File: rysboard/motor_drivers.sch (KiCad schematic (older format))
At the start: 26 parts, among them J15 Microfit_1x4, J16 Microfit_1x4, U2 ST L6470 28Pin, U3 ST L6470 28Pin

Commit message: rysboard: schematic cleanup done after kicad import
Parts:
- removed C10, C11: 47u, Capacitor_Tantalum_SMD:CP_EIA-7343-31_Kemet-D, symbol Device:CP
- removed C12, C2, C5, C6: 100n, Capacitor_SMD:C_0603_1608Metric, symbol Device:C
- removed C16: 220n, Capacitor_SMD:C_0805_2012Metric, symbol Device:C
- removed C3: 10u, Capacitor_SMD:C_1206_3216Metric, symbol Device:C
- removed J16: Microfit_1x4, Connector_Molex:Molex_Micro-Fit_3.0_43650-0415_1x04_P3.00mm_Vertical, symbol rysboard:Microfit_1x4
- removed R4: 27k1%, Resistor_SMD:R_0603_1608Metric, symbol Device:R
- removed U3: ST L6470 28Pin, symbol rysboard:ST_L6470_28Pin
- added C10: 10n, Capacitor_SMD:C_0603_1608Metric, symbol Device:C
- added C11: 100n, Capacitor_SMD:C_0603_1608Metric, symbol Device:C
- added C12, C13: 47u, Capacitor_Tantalum_SMD:CP_EIA-7343-31_Kemet-D, symbol Device:CP
- added C8: 10u, Capacitor_SMD:C_1206_3216Metric, symbol Device:C
- added C9: 220n, Capacitor_SMD:C_0805_2012Metric, symbol Device:C
- added J3: Motor R, Connector_Molex:Molex_Micro-Fit_3.0_43650-0415_1x04_P3.00mm_Vertical, symbol rysboard:Microfit_1x4
- added R1, R2: 10k, Resistor_SMD:R_0603_1608Metric, symbol Device:R
- added R5: 27k1%, Resistor_SMD:R_0603_1608Metric, symbol Device:R
- added U2: L6470, Package_SO:HTSSOP-28-1EP_4.4x9.7mm_P0.65mm_EP3.4x9.5mm_ThermalVias, symbol rysboard:ST_L6470_HTSSOP28
- C14: value 10u -> 100n; footprint Capacitor_SMD:C_1206_3216Metric -> Capacitor_SMD:C_0603_1608Metric
- C3: renamed from C13; value 10u -> 10n; footprint Capacitor_SMD:C_1206_3216Metric -> Capacitor_SMD:C_0603_1608Metric
- J2: renamed from J15; value Microfit_1x4 -> Motor L
- U1: renamed from U2; value ST L6470 28Pin -> L6470; footprint (none) -> Package_SO:HTSSOP-28-1EP_4.4x9.7mm_P0.65mm_EP3.4x9.5mm_ThermalVias; symbol rysboard:ST_L6470_28Pin -> rysboard:ST_L6470_HTSSOP28
- renumbered C15 to C2, C7 to C5, C8 to C6, C9 to C7, R5 to R4
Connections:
- net labels removed: VBOOT0, VBOOT1
- wire segments 124 -> 119
- no-connect marks 8 -> 6
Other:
- note added: "Pull-ups for STANDBY and BUSY flags (active low)"
- note removed: "Sterowniki silników krokowych"
- moved on the sheet: C2, C3, C5, C6, C7, D1, R3, R4

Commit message: rysboard: library cleanup, fix bad connector references
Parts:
- J2, J3: symbol rysboard:Microfit_1x4 -> Connector_Generic:Conn_01x04
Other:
- moved on the sheet: C13, C14, C6, C7
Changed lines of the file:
@@
 L Device:CP C6
 U 1 1 5EB9B840
-P 5175 3900
-F 0 "C6" H 5275 3910 60  0000 L BNN
-F 1 "47u" H 5275 3810 60  0000 L BNN
-F 2 "Capacitor_Tantalum_SMD:CP_EIA-7343-31_Kemet-D" H 5275 3810 60  0001 C CNN
-F 3 "" H 5275 3810 60  0000 C CNN
-	1    5175 3900
+P 5225 3900
+F 0 "C6" H 5325 3910 60  0000 L BNN
+F 1 "47u" H 5325 3810 60  0000 L BNN
+F 2 "Capacitor_Tantalum_SMD:CP_EIA-7343-31_Kemet-D" H 5325 3810 60  0001 C CNN
+F 3 "" H 5325 3810 60  0000 C CNN
+	1    5225 3900
 	1    0    0    -1
 $EndComp
@@
 L power:Vdrive #PWR09
 U 1 1 5E96DF0C
-P 5000 3450
-F 0 "#PWR09" H 4800 3300 50  0001 C CNN
-F 1 "Vdrive" H 5017 3623 50  0000 C CNN
-F 2 "" H 5000 3450 50  0001 C CNN
-F 3 "" H 5000 3450 50  0001 C CNN
-	1    5000 3450
+P 5025 3450
+F 0 "#PWR09" H 4825 3300 50  0001 C CNN
+F 1 "Vdrive" H 5042 3623 50  0000 C CNN
+F 2 "" H 5025 3450 50  0001 C CNN
+F 3 "" H 5025 3450 50  0001 C CNN
+	1    5025 3450
 	1    0    0    -1
 $EndComp
@@
 L Device:C C7
 U 1 1 5E95E4E7
-P 5500 3900
-F 0 "C7" H 5600 3925 60  0000 L BNN
-F 1 "100n" H 5600 3825 60  0000 L BNN
-F 2 "Capacitor_SMD:C_0603_1608Metric" H 5400 3990 60  0001 C CNN
-F 3 "" H 5400 3990 60  0001 C CNN
-	1    5500 3900
-	1    0    0    -1
-$EndComp
-Wire Wire Line
-	5000 3550 5000 3450
+P 5600 3900
+F 0 "C7" H 5700 3925 60  0000 L BNN
+F 1 "100n" H 5700 3825 60  0000 L BNN
+F 2 "Capacitor_SMD:C_0603_1608Metric" H 5500 3990 60  0001 C CNN
+F 3 "" H 5500 3990 60  0001 C CNN
+	1    5600 3900
+	1    0    0    -1
+$EndComp
+Wire Wire Line
+	5025 3550 5025 3450
 $Comp
 L Device:R R4
@@
 L power:GND #PWR010
 U 1 1 5E9B3268
-P 5000 4250
-F 0 "#PWR010" H 5000 4000 50  0001 C CNN
-F 1 "GND" H 5005 4077 50  0000 C CNN
-F 2 "" H 5000 4250 50  0001 C CNN
-F 3 "" H 5000 4250 50  0001 C CNN
-	1    5000 4250
+P 5025 4250
+F 0 "#PWR010" H 5025 4000 50  0001 C CNN
+F 1 "GND" H 5030 4077 50  0000 C CNN
+F 2 "" H 5025 4250 50  0001 C CNN
+F 3 "" H 5025 4250 50  0001 C CNN
+	1    5025 4250
 	1    0    0    -1
 $EndComp
@@
 Connection ~ 4825 3550
 Wire Wire Line
-	4825 3550 5000 3550
-Wire Wire Line
-	5175 3750 5175 3550
-Wire Wire Line
-	5500 3750 5500 3550
-Wire Wire Line
-	5500 3550 5175 3550
-Connection ~ 5175 3550
-Connection ~ 5000 3550
-Wire Wire Line
-	5000 3550 5175 3550
+	4825 3550 5025 3550
+Wire Wire Line
+	5225 3750 5225 3550
+Wire Wire Line
+	5600 3750 5600 3550
+Wire Wire Line
+	5600 3550 5225 3550
+Connection ~ 5225 3550
+Connection ~ 5025 3550
+Wire Wire Line
+	5025 3550 5225 3550
 Wire Wire Line
 	4825 4050 4825 4250
 Connection ~ 4825 4250
 Wire Wire Line
-	4825 4250 5000 4250
-Wire Wire Line
-	5500 4050 5500 4250
-Wire Wire Line
-	5500 4250 5175 4250
-Connection ~ 5000 4250
-Wire Wire Line
-	5175 4050 5175 4250
-Connection ~ 5175 4250
-Wire Wire Line
-	5175 4250 5000 4250
+	4825 4250 5025 4250
+Wire Wire Line
+	5600 4050 5600 4250
+Wire Wire Line
+	5600 4250 5225 4250
+Connection ~ 5025 4250
+Wire Wire Line
+	5225 4050 5225 4250
+Connection ~ 5225 4250
+Wire Wire Line
+	5225 4250 5025 4250
 Wire Wire Line
 	4425 3850 4425 3900
@@
 	4425 3900 4425 3950
 $Comp
-L rysboard:Microfit_1x4 J2
+L Connector_Generic:Conn_01x04 J2
 U 1 1 5EB6E00E
-P 4575 2250
-F 0 "J2" H 4625 2000 60  0000 R TNN
-F 1 "Motor L" H 4625 2500 60  0000 R BNN
-F 2 "Connector_Molex:Molex_Micro-Fit_3.0_43650-0415_1x04_P3.00mm_Vertical" H 4825 2400 60  0001 C CNN
-F 3 "" H 4825 2400 60  0001 C CNN
-	1    4575 2250
-	-1   0    0    1
+P 4525 2200
+F 0 "J2" H 4525 2375 50  0000 C CNN
+F 1 "Motor L" H 4525 1900 50  0000 C CNN
+F 2 "Connector_Molex:Molex_Micro-Fit_3.0_43650-0415_1x04_P3.00mm_Vertical" H 4775 2350 50  0001 C CNN
+F 3 "" H 4775 2350 50  0001 C CNN
+	1    4525 2200
+	1    0    0    -1
 $EndComp
 Wire Wire Line
@@
 L Device:CP C13
 U 1 1 5EAE3CD8
-P 9675 3900
-F 0 "C13" H 9775 3910 60  0000 L BNN
-F 1 "47u" H 9775 3810 60  0000 L BNN
-F 2 "Capacitor_Tantalum_SMD:CP_EIA-7343-31_Kemet-D" H 9775 3810 60  0001 C CNN
-F 3 "" H 9775 3810 60  0000 C CNN
-	1    9675 3900
+P 9725 3900
+F 0 "C13" H 9825 3910 60  0000 L BNN
+F 1 "47u" H 9825 3810 60  0000 L BNN
+F 2 "Capacitor_Tantalum_SMD:CP_EIA-7343-31_Kemet-D" H 9825 3810 60  0001 C CNN
+F 3 "" H 9825 3810 60  0000 C CNN
+	1    9725 3900
 	1    0    0    -1
 $EndComp
@@
 L power:Vdrive #PWR015
 U 1 1 5EAE3CE4
-P 9500 3450
-F 0 "#PWR015" H 9300 3300 50  0001 C CNN
-F 1 "Vdrive" H 9517 3623 50  0000 C CNN
-F 2 "" H 9500 3450 50  0001 C CNN
-F 3 "" H 9500 3450 50  0001 C CNN
-	1    9500 3450
+P 9525 3450
+F 0 "#PWR015" H 9325 3300 50  0001 C CNN
+F 1 "Vdrive" H 9542 3623 50  0000 C CNN
+F 2 "" H 9525 3450 50  0001 C CNN
+F 3 "" H 9525 3450 50  0001 C CNN
+	1    9525 3450
 	1    0    0    -1
 $EndComp
@@
 L Device:C C14
 U 1 1 5EAE3CEA
-P 10000 3900
-F 0 "C14" H 10100 3925 60  0000 L BNN
-F 1 "100n" H 10100 3825 60  0000 L BNN
-F 2 "Capacitor_SMD:C_0603_1608Metric" H 9900 3990 60  0001 C CNN
-F 3 "" H 9900 3990 60  0001 C CNN
-	1    10000 3900
-	1    0    0    -1
-$EndComp
-Wire Wire Line
-	9500 3550 9500 3450
+P 10100 3900
+F 0 "C14" H 10200 3925 60  0000 L BNN
+F 1 "100n" H 10200 3825 60  0000 L BNN
+F 2 "Capacitor_SMD:C_0603_1608Metric" H 10000 3990 60  0001 C CNN
+F 3 "" H 10000 3990 60  0001 C CNN
+	1    10100 3900
+	1    0    0    -1
+$EndComp
+Wire Wire Line
+	9525 3550 9525 3450
 $Comp
 L Device:R R6
@@
 L power:GND #PWR016
 U 1 1 5EAE3CF7
-P 9500 4250
-F 0 "#PWR016" H 9500 4000 50  0001 C CNN
-F 1 "GND" H 9505 4077 50  0000 C CNN
-F 2 "" H 9500 4250 50  0001 C CNN
-F 3 "" H 9500 4250 50  0001 C CNN
-	1    9500 4250
+P 9525 4250
+F 0 "#PWR016" H 9525 4000 50  0001 C CNN
+F 1 "GND" H 9530 4077 50  0000 C CNN
+F 2 "" H 9525 4250 50  0001 C CNN
+F 3 "" H 9525 4250 50  0001 C CNN
+	1    9525 4250
 	1    0    0    -1
 $EndComp
@@
 Connection ~ 9325 3550
 Wire Wire Line
-	9325 3550 9500 3550
-Wire Wire Line
-	9675 3750 9675 3550
-Wire Wire Line
-	10000 3750 10000 3550
-Wire Wire Line
-	10000 3550 9675 3550
-Connection ~ 9675 3550
-Connection ~ 9500 3550
-Wire Wire Line
-	9500 3550 9675 3550
+	9325 3550 9525 3550
+Wire Wire Line
+	9725 3750 9725 3550
+Wire Wire Line
+	10100 3750 10100 3550
+Wire Wire Line
+	10100 3550 9725 3550
+Connection ~ 9725 3550
+Connection ~ 9525 3550
+Wire Wire Line
+	9525 3550 9725 3550
 Wire Wire Line
 	9325 4050 9325 4250
 Connection ~ 9325 4250
 Wire Wire Line
-	9325 4250 9500 4250
-Wire Wire Line
-	10000 4050 10000 4250
-Wire Wire Line
-	10000 4250 9675 4250
-Connection ~ 9500 4250
-Wire Wire Line
-	9675 4050 9675 4250
-Connection ~ 9675 4250
-Wire Wire Line
-	9675 4250 9500 4250
+	9325 4250 9525 4250
+Wire Wire Line
+	10100 4050 10100 4250
+Wire Wire Line
+	10100 4250 9725 4250
+Connection ~ 9525 4250
+Wire Wire Line
+	9725 4050 9725 4250
+Connection ~ 9725 4250
+Wire Wire Line
+	9725 4250 9525 4250
 Wire Wire Line
 	8925 3850 8925 3900
@@
 	8925 3900 8925 3950
 $Comp
-L rysboard:Microfit_1x4 J3
+L Connector_Generic:Conn_01x04 J3
 U 1 1 5EAE3D14
-P 9075 2250
-F 0 "J3" H 9125 2000 60  0000 R TNN
-F 1 "Motor R" H 9125 2500 60  0000 R BNN
-F 2 "Connector_Molex:Molex_Micro-Fit_3.0_43650-0415_1x04_P3.00mm_Vertical" H 9325 2400 60  0001 C CNN
-F 3 "" H 9325 2400 60  0001 C CNN
-	1    9075 2250
-	-1   0    0    1
-$EndComp
-Wire Wire Line
+P 9025 2200
+F 0 "J3" H 9025 2375 50  0000 C CNN
+F 1 "Motor R" H 9025 1900 50  0000 C CNN
+F 2 "Connector_Molex:Molex_Micro-Fit_3.0_43650-0415_1x04_P3.00mm_Vertical" H 9275 2350 50  0001 C CNN
+F 3 "" H 9275 2350 50  0001 C CNN
+	1    9025 2200
+	1    0    0    -1
+$EndComp
+Wire Wire Line

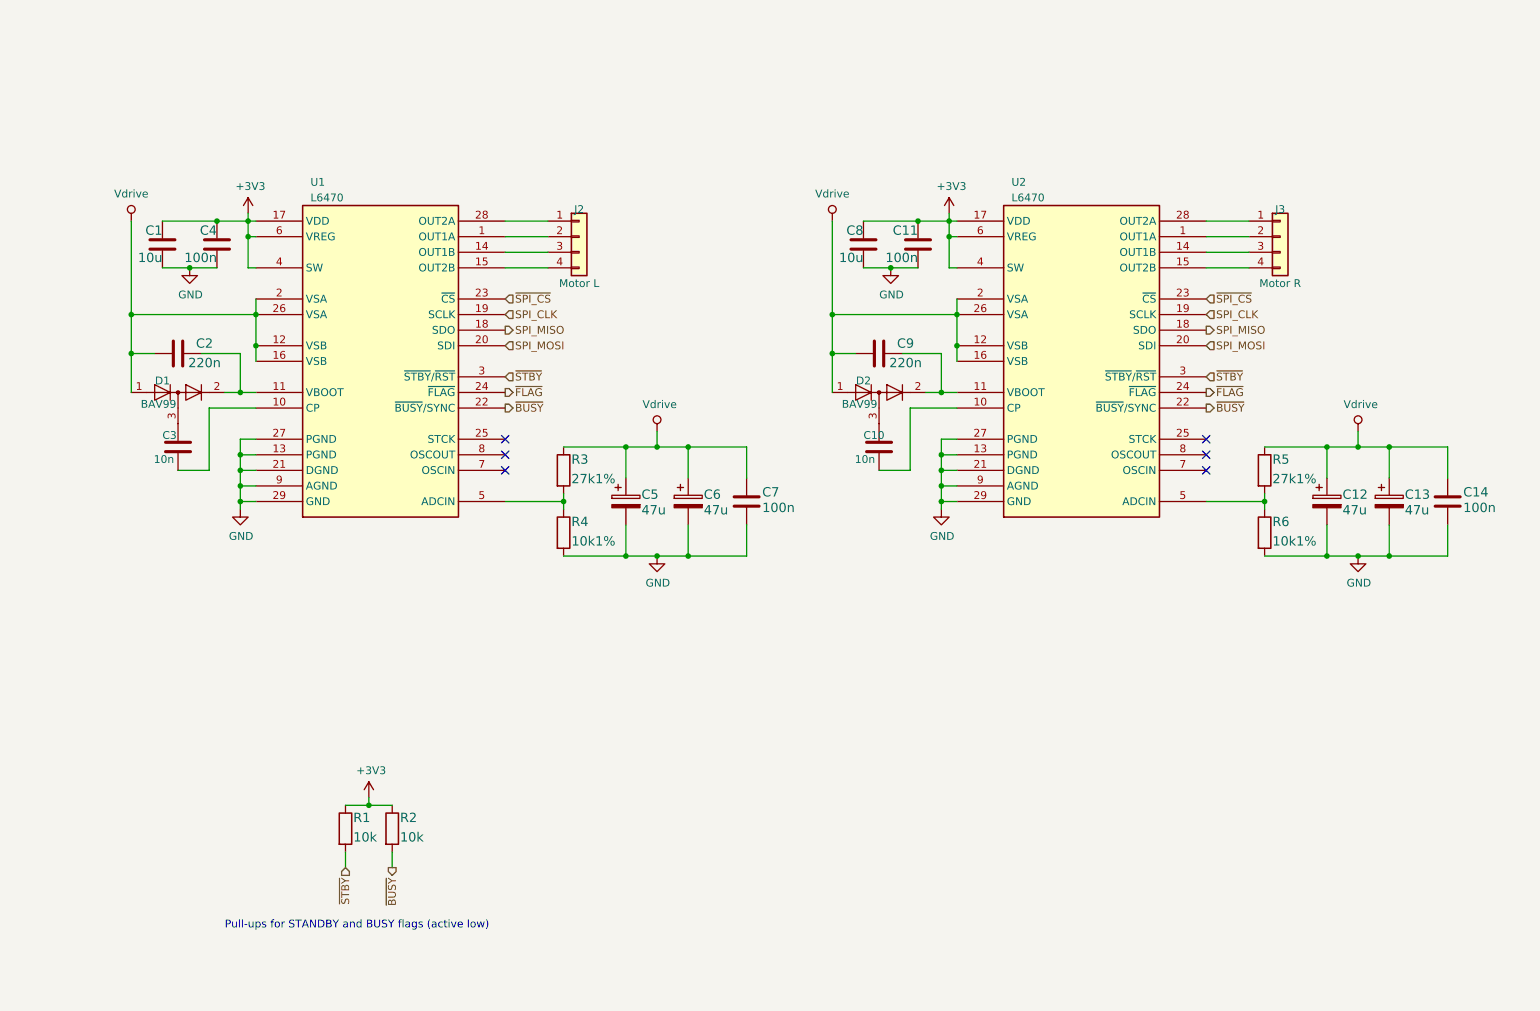
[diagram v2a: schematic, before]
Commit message: rysboard: 4.2 schematic
Change the I2C buses and GPIOs used
Fix L6470 connections
Change ADC to 4-channel
Add 2 user LEDs
Add I2C pullups
Add serial connector
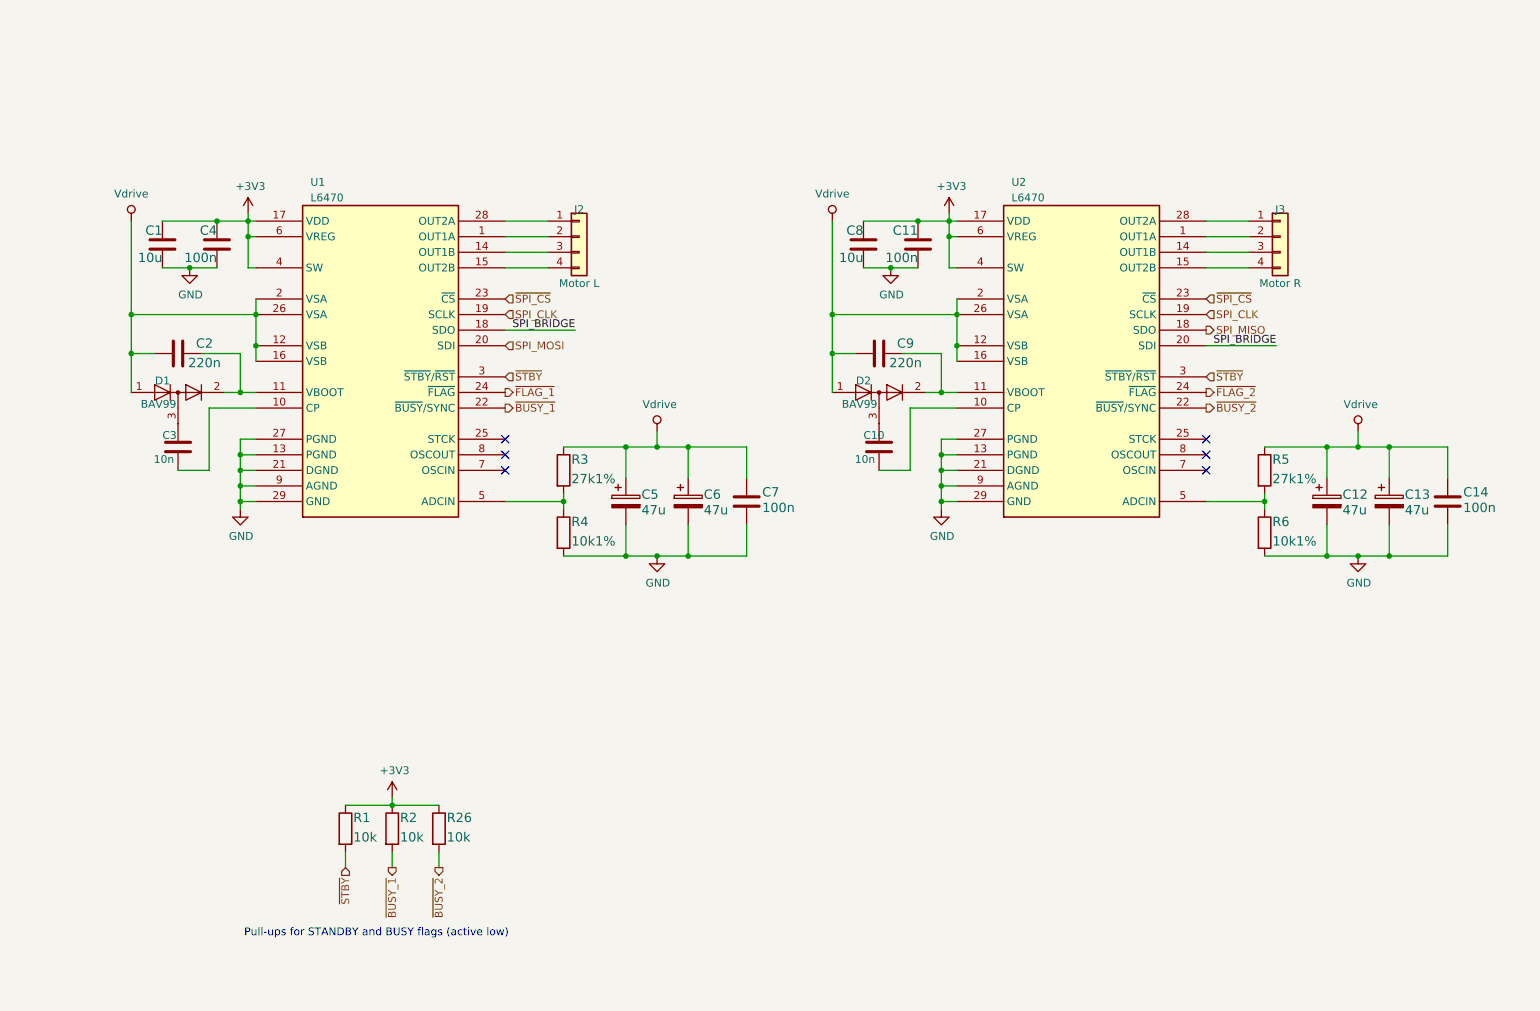
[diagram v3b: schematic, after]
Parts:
- added R26: 10k, Resistor_SMD:R_0603_1608Metric, symbol Device:R
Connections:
- net +3V3: now also R26.1
- net SPI_MISO: no longer U1.18 (SDO)
- net SPI_MOSI: no longer U2.20 (SDI)
- net ~BUSY renamed ~BUSY_1
- net ~BUSY_1: no longer U2.22 (~BUSY~/SYNC)
- net ~FLAG renamed ~FLAG_1
- net ~FLAG_1: no longer U2.24 (~FLAG)
- new net SPI_BRIDGE: U1.18 (SDO), U2.20 (SDI)
- new net ~BUSY_2: R26.2, U2.22 (~BUSY~/SYNC)
- new net ~FLAG_2: U2.24 (~FLAG)
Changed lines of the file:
@@
 Connection ~ 2350 3600
 Text HLabel 4050 3200 2    50   Output ~ 0
-~FLAG
+~FLAG_1
 Text HLabel 4050 3300 2    50   Output ~ 0
-~BUSY
+~BUSY_1
 Text HLabel 4050 2600 2    50   Input ~ 0
 ~SPI_CS
 Text HLabel 4050 2700 2    50   Input ~ 0
 SPI_CLK
-Text HLabel 4050 2800 2    50   Output ~ 0
-SPI_MISO
 Text HLabel 4050 2900 2    50   Input ~ 0
 SPI_MOSI
@@
 L power:+3V3 #PWR08
 U 1 1 5E813E65
-P 3175 5800
-F 0 "#PWR08" H 3175 5650 50  0001 C CNN
-F 1 "+3V3" H 3190 5973 50  0000 C CNN
-F 2 "" H 3175 5800 50  0001 C CNN
-F 3 "" H 3175 5800 50  0001 C CNN
-	1    3175 5800
+P 3325 5800
+F 0 "#PWR08" H 3325 5650 50  0001 C CNN
+F 1 "+3V3" H 3340 5973 50  0000 C CNN
+F 2 "" H 3325 5800 50  0001 C CNN
+F 3 "" H 3325 5800 50  0001 C CNN
+	1    3325 5800
 	1    0    0    -1
 $EndComp
 Text HLabel 3325 6250 3    50   Output ~ 0
-~BUSY
+~BUSY_1
 Text HLabel 3025 6250 3    50   Input ~ 0
 ~STBY
@@
 $EndComp
 Wire Wire Line
-	3025 5850 3175 5850
-Wire Wire Line
-	3175 5850 3175 5800
-Wire Wire Line
-	3325 5850 3175 5850
-Connection ~ 3175 5850
+	3325 5850 3325 5800
 Wire Wire Line
 	3325 6150 3325 6250
 Wire Wire Line
 	3025 6150 3025 6250
-Text Notes 2250 6650 0    50   ~ 0
+Text Notes 2375 6700 0    50   ~ 0
 Pull-ups for STANDBY and BUSY flags (active low)
 $Comp
@@
 Connection ~ 6850 3600
 Text HLabel 8550 3200 2    50   Output ~ 0
-~FLAG
+~FLAG_2
 Text HLabel 8550 3300 2    50   Output ~ 0
-~BUSY
+~BUSY_2
 Text HLabel 8550 2600 2    50   Input ~ 0
 ~SPI_CS
@@
 Text HLabel 8550 2800 2    50   Output ~ 0
 SPI_MISO
-Text HLabel 8550 2900 2    50   Input ~ 0
-SPI_MOSI
 $Comp
 L Device:R R5
@@
 NoConn ~ 8550 3600
 NoConn ~ 8550 3700
+Wire Wire Line
+	4050 2800 4500 2800
+Text Label 4500 2800 2    50   ~ 0
+SPI_BRIDGE
+Wire Wire Line
+	8550 2900 9000 2900
+Text Label 9000 2900 2    50   ~ 0
+SPI_BRIDGE
+Text HLabel 3625 6250 3    50   Output ~ 0
+~BUSY_2
+$Comp
+L Device:R R26
+U 1 1 5ECB66DC
+P 3625 6000
+F 0 "R26" H 3675 6035 60  0000 L BNN
+F 1 "10k" H 3675 5910 60  0000 L BNN
+F 2 "Resistor_SMD:R_0603_1608Metric" H 3535 5950 60  0001 C CNN
+F 3 "" H 3535 5950 60  0000 C CNN
+	1    3625 6000
+	1    0    0    -1
+$EndComp
+Wire Wire Line
+	3625 6150 3625 6250
+Wire Wire Line
+	3325 5850 3625 5850
+Connection ~ 3325 5850
+Wire Wire Line
+	3025 5850 3325 5850
 $EndSCHEMATC
